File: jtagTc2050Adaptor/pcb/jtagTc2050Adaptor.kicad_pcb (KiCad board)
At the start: 2 copper layers, 48.1 x 34.3 mm, 29 parts, among them CON1 10PIN_JTAG_SWD, P1 CONN_01X02, P10 CONN_01X03, P2 CONN_01X01, P3 CONN_01X03, P4 CONN_01X03, P5 USB_OTG, P6 CONN_02X10, P7 CONN_02X03, P9 CONN_01X03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

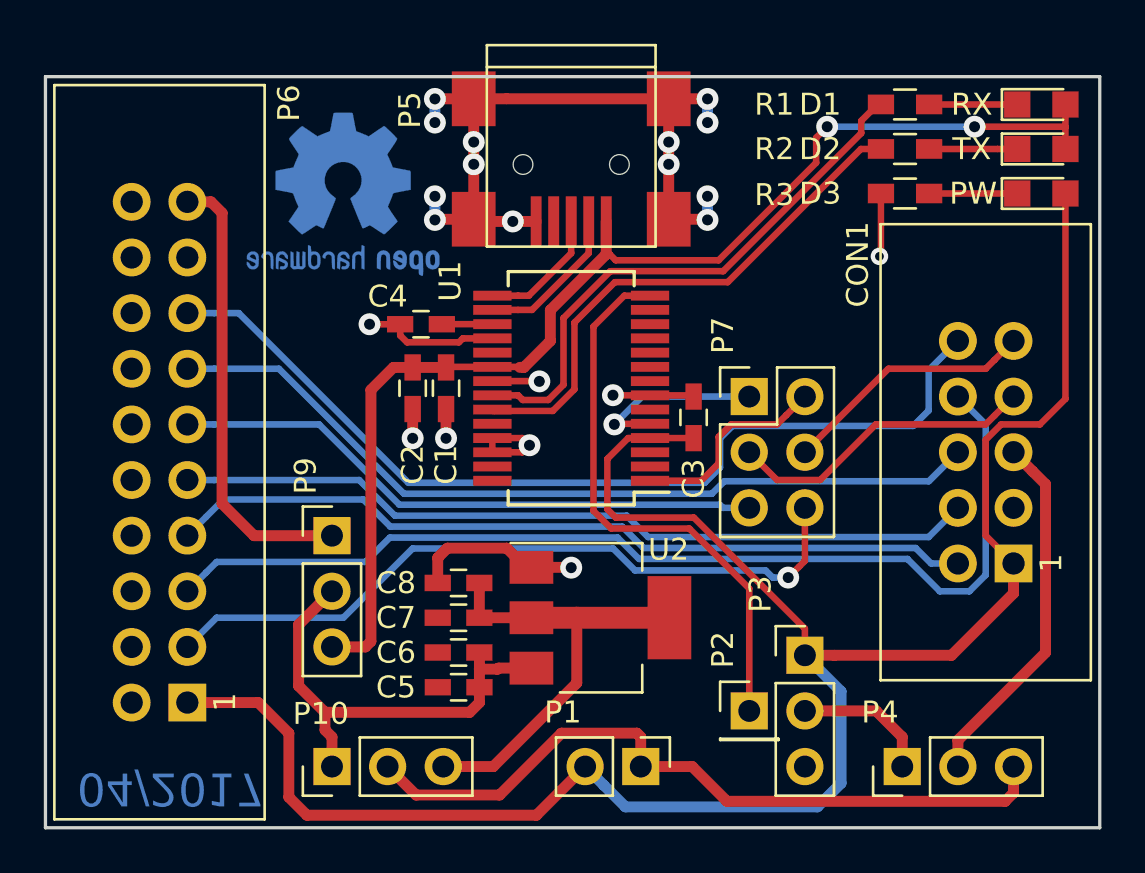
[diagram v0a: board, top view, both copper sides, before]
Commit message: finished some layouts
added pcb numbering and revision
added a pcb list
orderes the pcbs
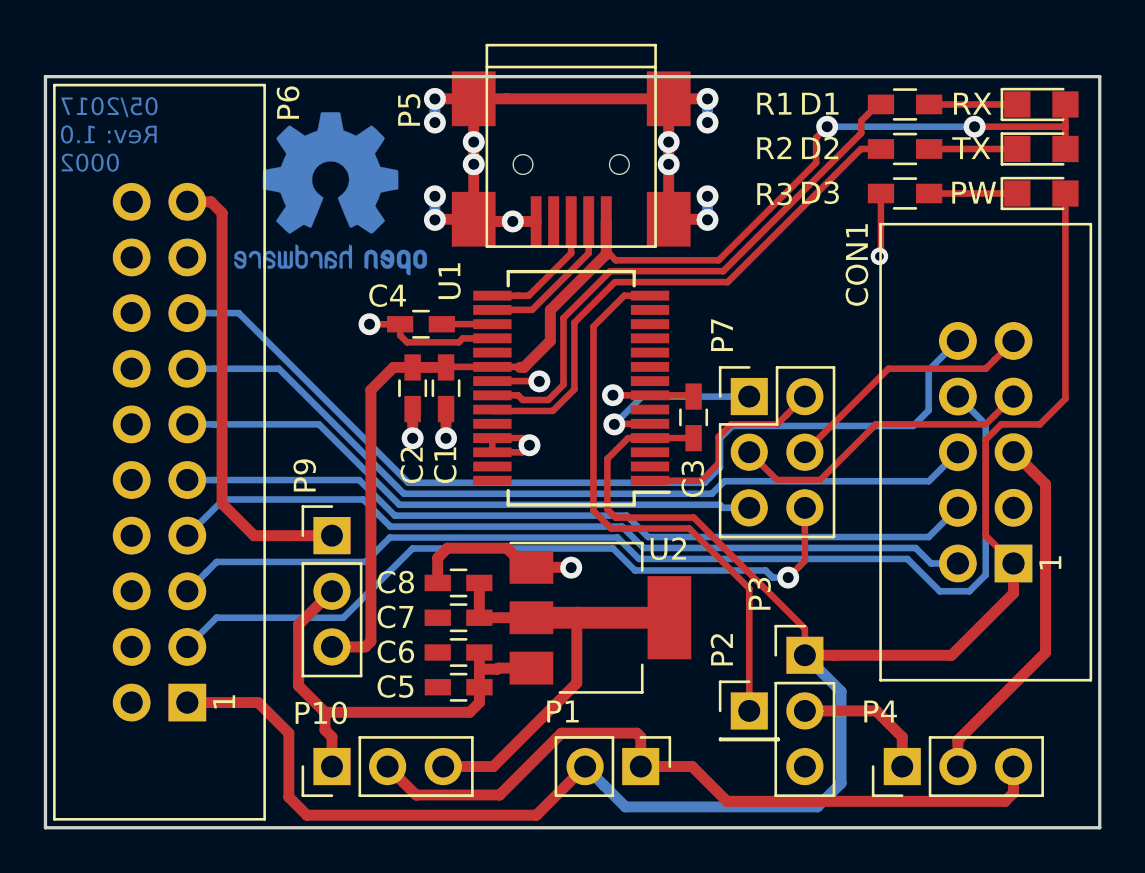
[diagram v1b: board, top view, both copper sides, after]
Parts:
- moved REF*** 0.57 mm to (65.2, 70.7)
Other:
- board text added: "05/2017 Rev: 1.0 0002"
- board text removed: "04/2017"
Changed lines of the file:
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@@
-(kicad_pcb (version 20170123) (host pcbnew "(2017-04-22 revision b38541345)-makepkg")
+(kicad_pcb (version 20170123) (host pcbnew "(2017-05-12 revision b823d0b78)-makepkg")
   (general
     (links 75)
@@
   )
   (page A4)
+  (title_block
+    (title jtagTc2050Adaptor)
+    (date 2017-05-13)
+    (rev 1.0)
+    (company shimatta)
+  )
   (layers
     (0 F.Cu signal)
@@
       (layerselection 0x010fc_ffffffff)
       (usegerberextensions true)
-      (excludeedgelayer false)
+      (excludeedgelayer true)
       (linewidth 0.100000)
-      (plotframeref true)
+      (plotframeref false)
       (viasonmask false)
       (mode 1)
@@
       (padsonsilk false)
       (subtractmaskfromsilk false)
-      (outputformat 4)
+      (outputformat 1)
       (mirror false)
-      (drillshape 2)
+      (drillshape 0)
       (scaleselection 1)
-      (outputdirectory doc))
+      (outputdirectory gerber))
   )
   (net 0 "")
@@
   )
   (module Symbols:OSHW-Logo2_9.8x8mm_Copper (layer B.Cu)
-    (at 65.786 70.7644 180)
+    (at 65.2145 70.739 180)
     (descr "Open Source Hardware Symbol")
     (tags "Logo Symbol OSHW")
@@
     (model ${KISYS3DMOD}/TO_SOT_Packages_SMD.3dshapes/SOT-223.wrl
       (at (xyz 0 0 0))
-      (scale (xyz 0.4 0.4 0.4))
-      (rotate (xyz 0 0 90))
+      (scale (xyz 1 1 1))
+      (rotate (xyz 0 0 0))
     )
   )
@@
     )
   )
-  (gr_text 04/2017 (at 57.912 97.917 180) (layer B.Cu)
-    (effects (font (size 1.5 1.5) (thickness 0.3)) (justify mirror))
+  (gr_text "05/2017\nRev: 1.0\n0002" (at 52.832 68.072) (layer B.Cu)
+    (effects (font (size 0.8 0.8) (thickness 0.2)) (justify right mirror))
   )
   (gr_line (start 66.4845 86.36) (end 66.8655 86.36) (layer B.SilkS) (width 0.2))
